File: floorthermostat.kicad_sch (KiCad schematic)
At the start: 26 parts, among them J1 Conn_01x03_Socket, J2 spi7segdisp, J3 ProgLoad, Q1 BC549, SW1 SW_Push, SW2 SW_Push, U1 ESP32-WROOM-32, U2 S202S02, U3 BD33FC0FP, U4 DS18B20

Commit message: Added labels for esp, about the spi display.
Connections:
- net CLK: now also U1.30 (IO18)
- net DIN: now also U1.31 (IO19)
- net LOAD: now also U1.29 (IO5)
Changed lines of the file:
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@@
+	(wire
+		(pts
+			(xy 128.27 80.01) (xy 135.89 80.01)
+		)
+		(stroke
+			(width 0)
+			(type default)
+		)
+	)
 	(wire
 		(pts
@@
 	(wire
 		(pts
+			(xy 128.27 82.55) (xy 135.89 82.55)
+		)
+		(stroke
+			(width 0)
+			(type default)
+		)
+	)
+	(wire
+		(pts
 			(xy 175.26 72.39) (xy 175.26 76.2)
 		)
@@
 		(pts
 			(xy 200.66 36.83) (xy 213.36 36.83)
+		)
+		(stroke
+			(width 0)
+			(type default)
+		)
+	)
+	(wire
+		(pts
+			(xy 128.27 62.23) (xy 135.89 62.23)
 		)
 		(stroke
@@
 		)
 	)
+	(label "LOAD"
+		(at 135.89 62.23 180)
+		(fields_autoplaced yes)
+		(effects
+			(font
+				(size 1.27 1.27)
+			)
+			(justify right bottom)
+		)
+	)
 	(label "SETUP"
 		(at 135.89 67.31 180)
@@
 		)
 	)
+	(label "CLK"
+		(at 135.89 80.01 180)
+		(fields_autoplaced yes)
+		(effects
+			(font
+				(size 1.27 1.27)
+			)
+			(justify right bottom)
+		)
+	)
 	(label "TXD0/IO1"
 		(at 213.36 36.83 180)
@@
 		(fields_autoplaced yes)
 		(effects
+			(font
+				(size 1.27 1.27)
+			)
+			(justify right bottom)
+		)
+	)
+	(label "DIN"
+		(at 135.89 82.55 180)
+		(fields_autoplaced yes)
+		(effects

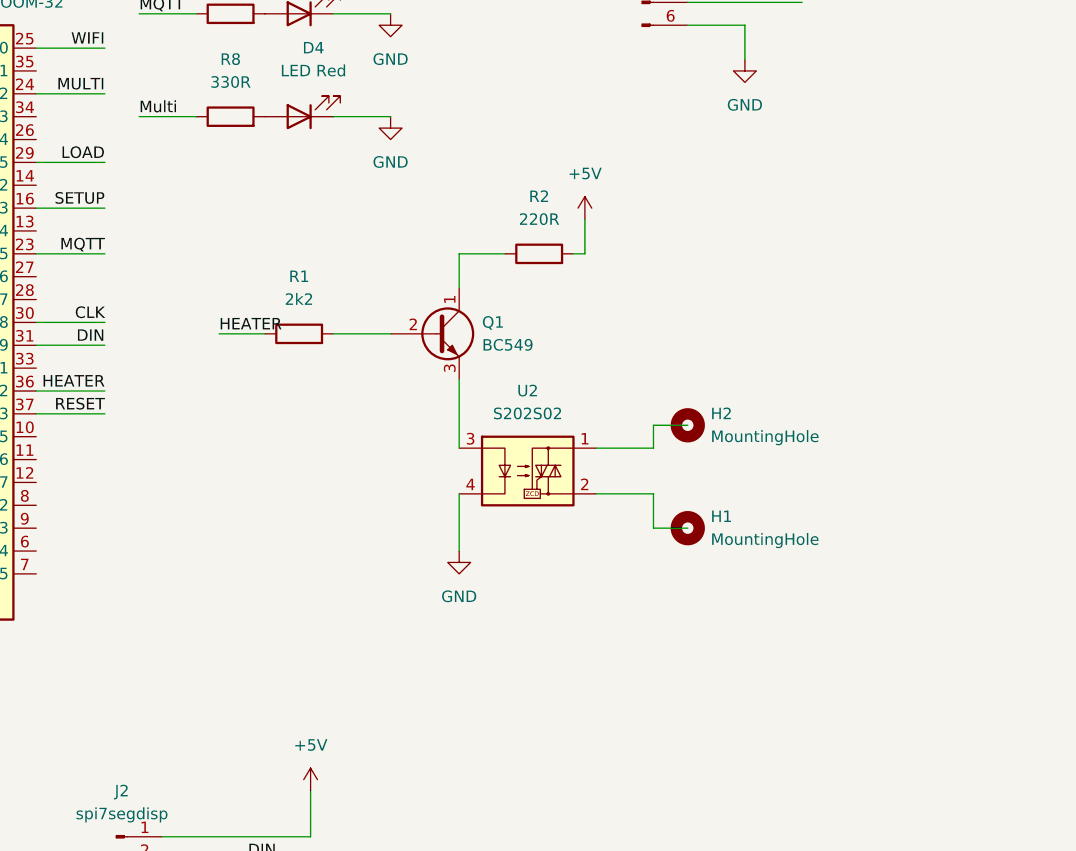
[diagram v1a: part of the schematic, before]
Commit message: Added ldr for display brightness control.
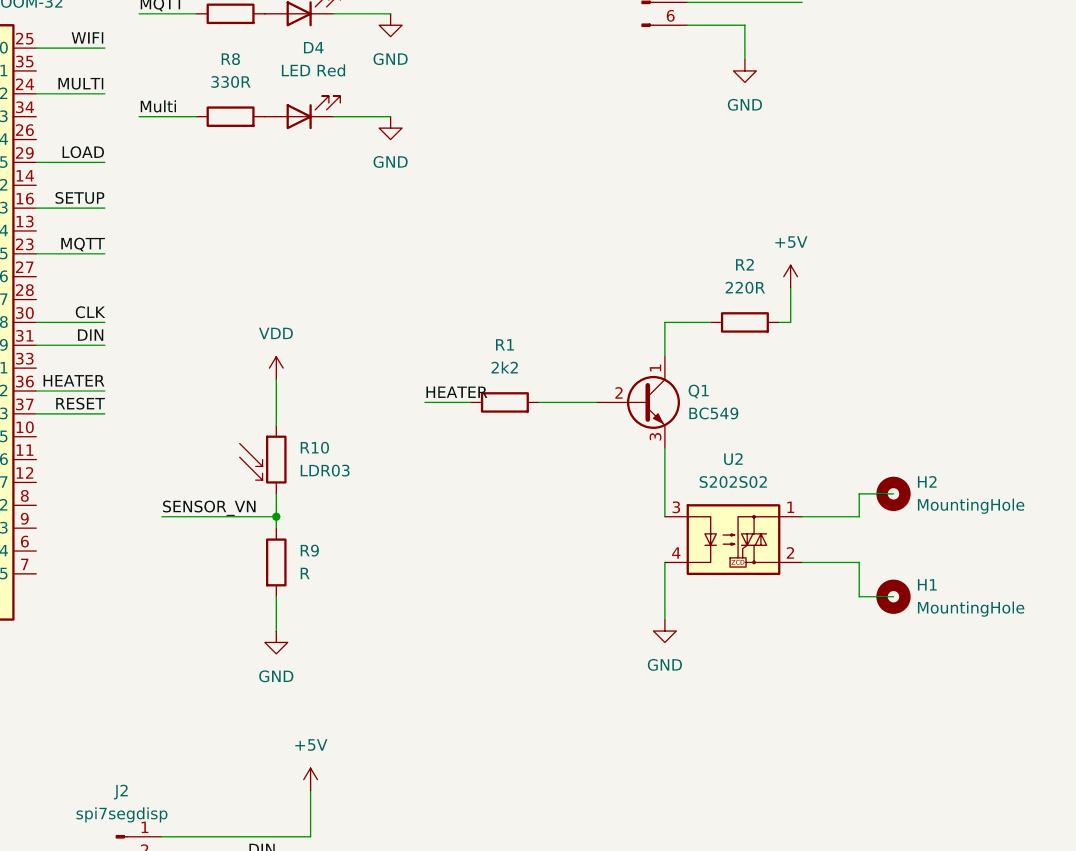
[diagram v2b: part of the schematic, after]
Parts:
- added R10: LDR03, OptoDevice:R_LDR_10x8.5mm_P7.6mm_Vertical, symbol Sensor_Optical:LDR03
- added R9: R, symbol Device:R
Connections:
- net GND: now also R9.2
- net VDD: now also R10.1
- new net SENSOR_VN: R10.2, R9.1
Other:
- moved on the sheet: H1, H2, Q1, R1, R2, U2

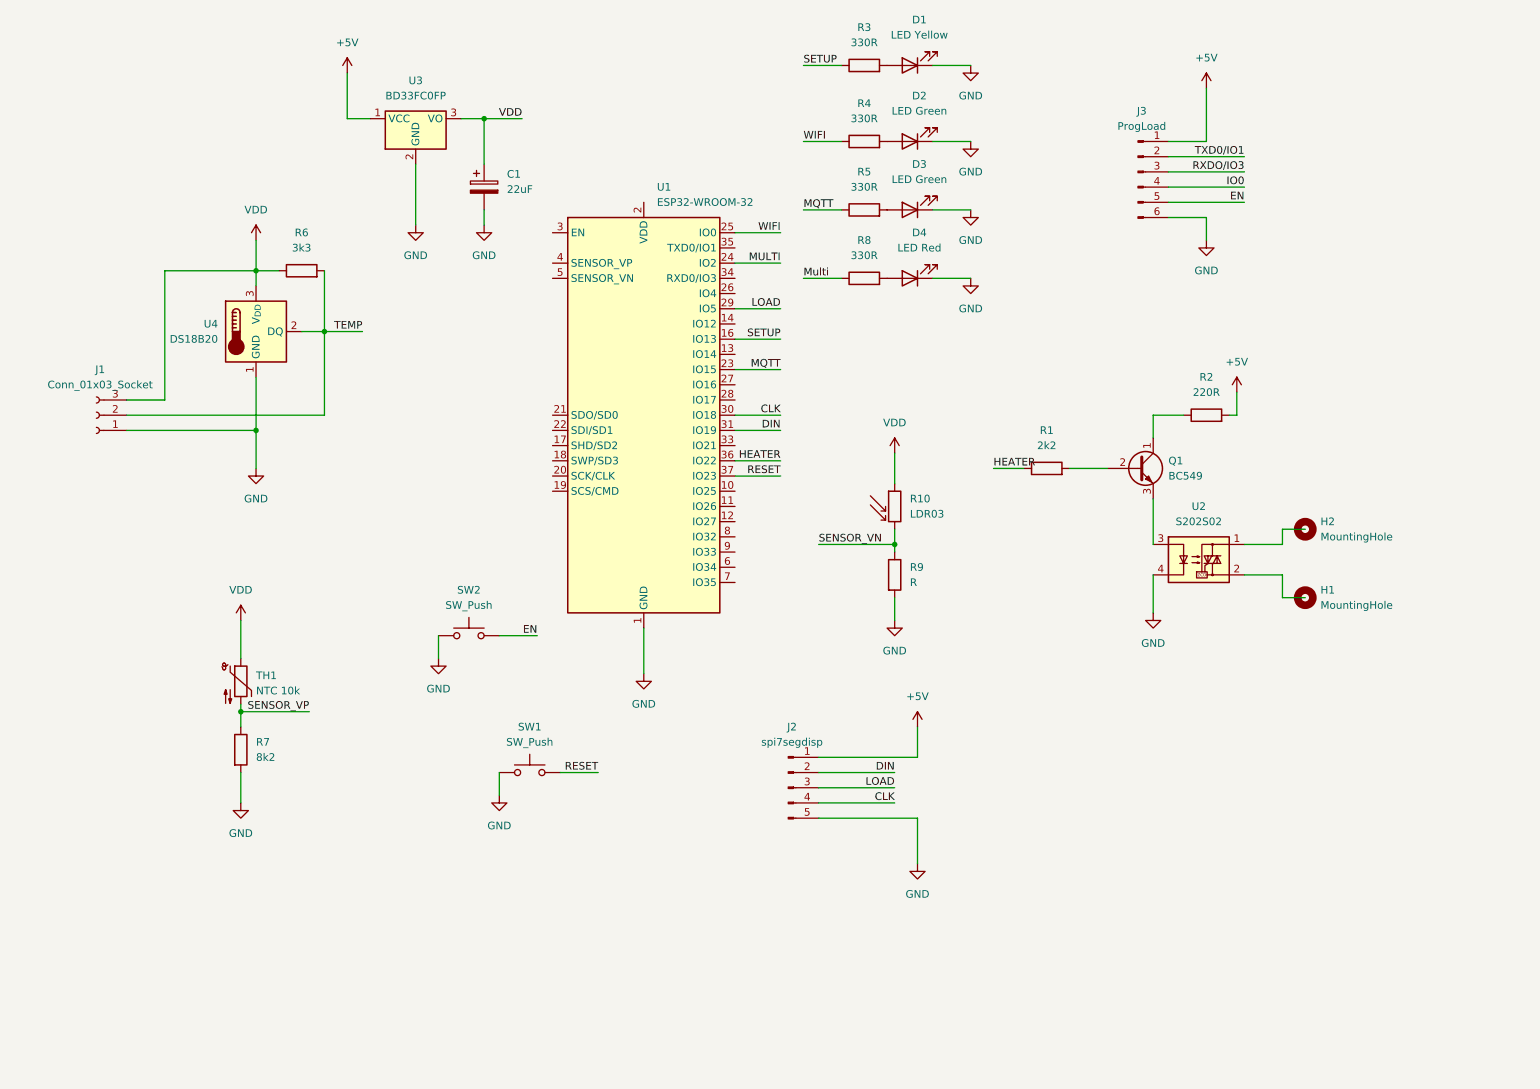
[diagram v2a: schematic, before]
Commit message: fixed ssr control bug. Added 2 filtering capasitors. Defined some component footprints.
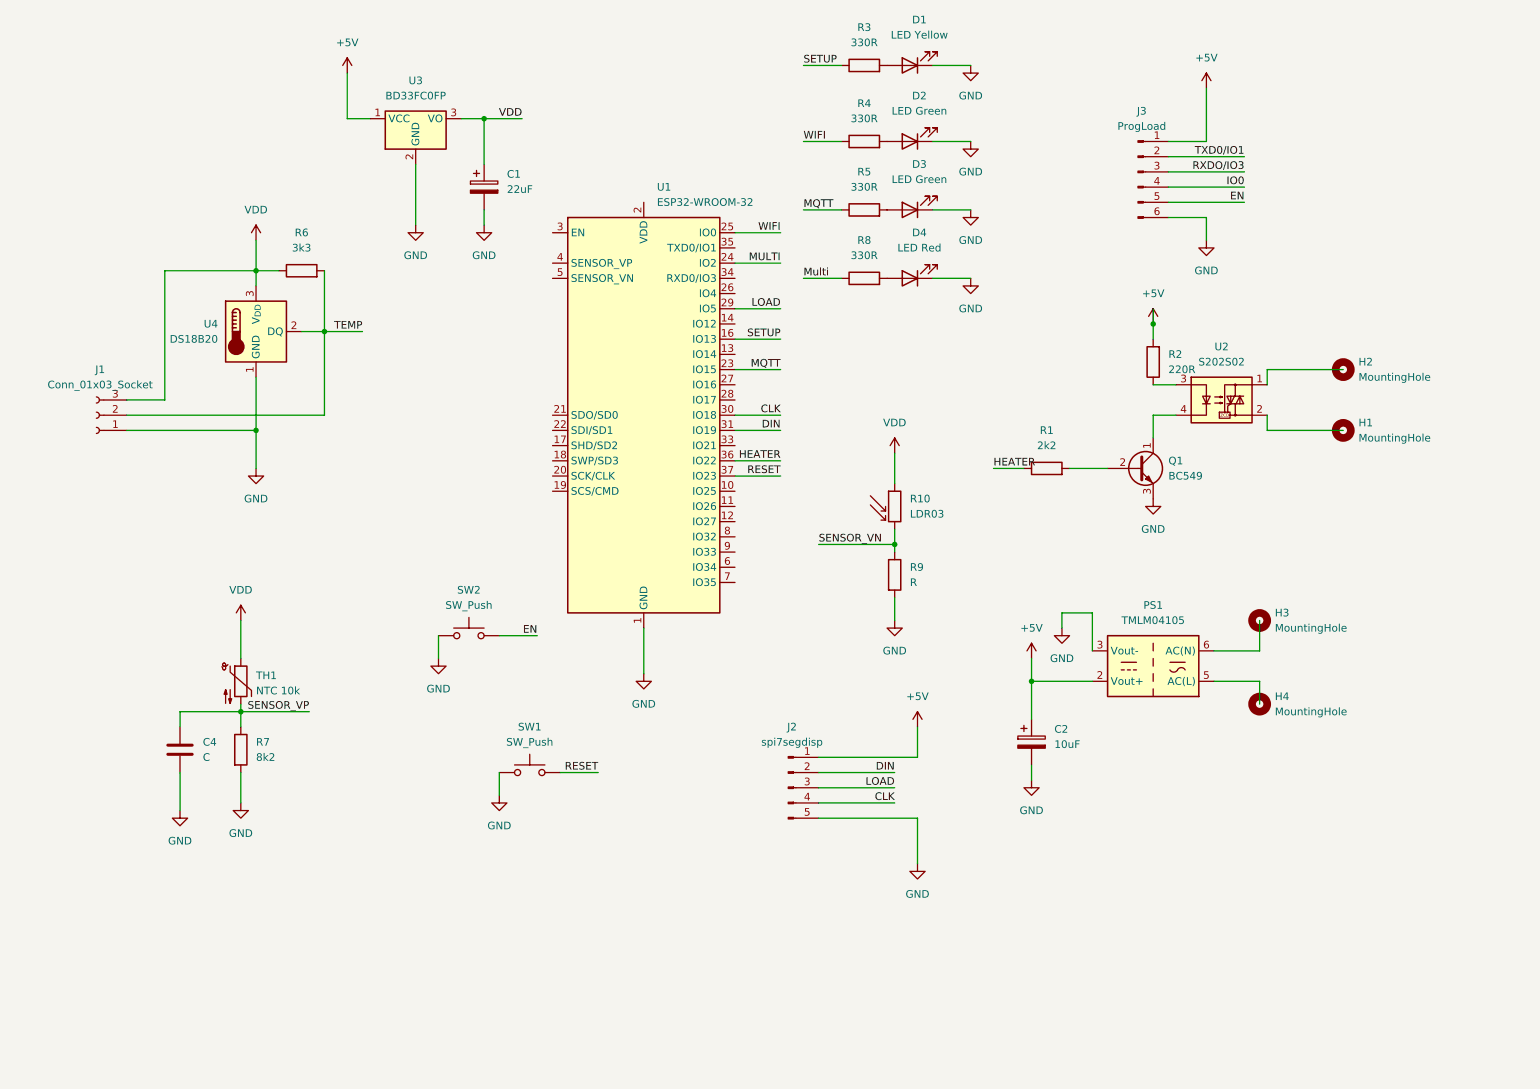
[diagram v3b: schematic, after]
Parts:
- added C2: 10uF, Capacitor_THT:CP_Axial_L10.0mm_D4.5mm_P15.00mm_Horizontal, symbol Device:C_Polarized
- added C4: C, Capacitor_THT:CP_Axial_L10.0mm_D6.0mm_P15.00mm_Horizontal, symbol Device:C
- added H3, H4: MountingHole, symbol Mechanical:MountingHole
- added PS1: TMLM04105, Converter_ACDC:Converter_ACDC_TRACO_TMLM-04_THT, symbol Converter_ACDC:TMLM04105
- C1: footprint (none) -> Capacitor_THT:CP_Axial_L10.0mm_D4.5mm_P15.00mm_Horizontal
- D1, D2, D3, D4: footprint (none) -> LED_THT:LED_D5.0mm
- R1: footprint (none) -> Resistor_THT:R_Axial_DIN0207_L6.3mm_D2.5mm_P15.24mm_Horizontal
- R2, R3, R4, R5, R6, R7, R8, R9: footprint (none) -> Resistor_THT:R_Axial_DIN0207_L6.3mm_D2.5mm_P2.54mm_Vertical
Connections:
- net +5V: now also C2.1, PS1.2 (Vout+)
- net GND: now also Q1.3 (E), C2.2, C4.2, PS1.3 (Vout-); no longer U2.4
- net SENSOR_VP: now also C4.1
- net at R2.1: now also U2.3; no longer Q1.1 (C)
- new net: Q1.1 (C), U2.4
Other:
- moved on the sheet: H1, H2, R2, U2

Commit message: Added many footprints.
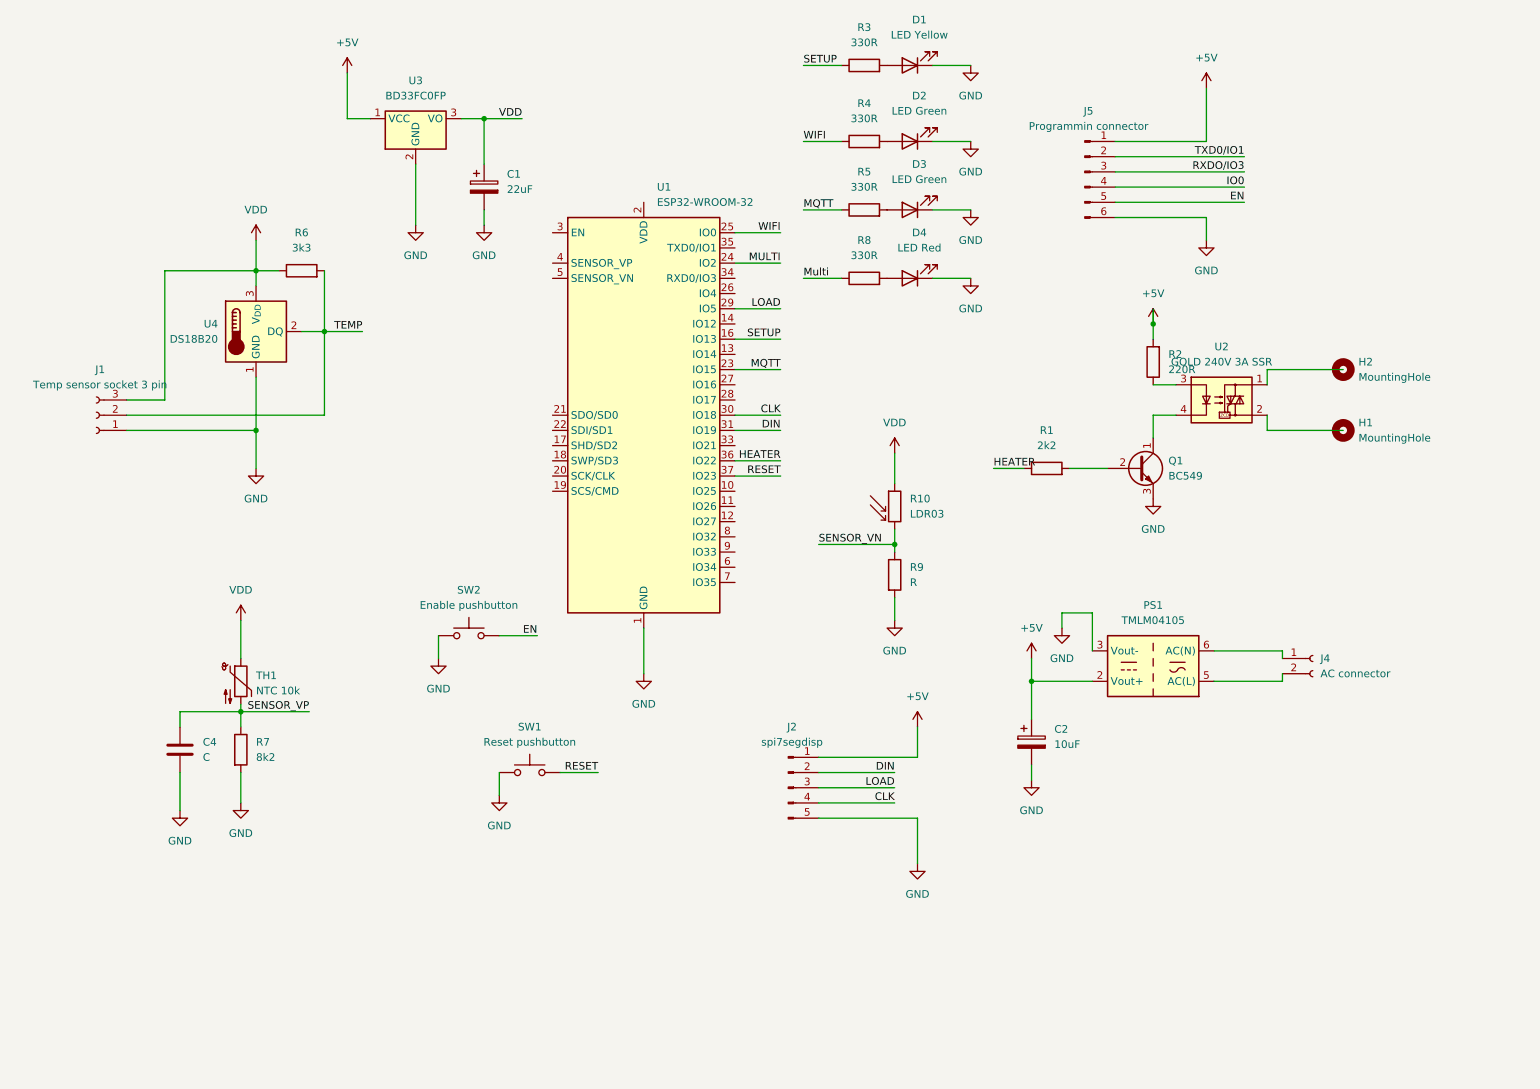
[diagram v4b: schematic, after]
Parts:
- removed H3, H4: MountingHole, symbol Mechanical:MountingHole
- removed J3: ProgLoad, symbol Connector:Conn_01x06_Pin
- added J4: AC connector, symbol Connector:Conn_01x02_Socket
- added J5: Programmin connector, Connector_PinHeader_2.54mm:PinHeader_1x06_P2.54mm_Vertical, symbol Connector:Conn_01x06_Pin
- H1: footprint (none) -> customparts:china_5v_acdc
- H2: footprint (none) -> Relay_THT:Relay_NCR_HHG1D-1
- J1: value Conn_01x03_Socket -> Temp sensor socket 3 pin; footprint (none) -> Connector_PinSocket_2.54mm:PinSocket_1x03_P2.54mm_Horizontal
- J2: footprint (none) -> Connector_PinHeader_2.54mm:PinHeader_1x05_P2.54mm_Vertical
- PS1: footprint Converter_ACDC:Converter_ACDC_TRACO_TMLM-04_THT -> customparts:china_5v_acdc
- SW1: value SW_Push -> Reset pushbutton; footprint (none) -> Button_Switch_THT:SW_PUSH_6mm_H5mm
- SW2: value SW_Push -> Enable pushbutton; footprint (none) -> Button_Switch_THT:SW_PUSH_6mm_H5mm
- U2: value S202S02 -> GOLD 240V 3A SSR; footprint Package_SIP:SIP4_Sharp-SSR_P7.62mm_Straight -> Relay_THT:Relay_NCR_HHG1D-1
- U3: footprint Package_TO_SOT_SMD:TO-252-2 -> Package_TO_SOT_THT:TO-262-3_Vertical
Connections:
- net +5V: now also J5.1 (Pin_1)
- net EN: now also J5.5 (Pin_5)
- net GND: now also J5.6 (Pin_6)
- net IO0: now also J5.4 (Pin_4)
- net RXDO/IO3: now also J5.3 (Pin_3)
- net TXD0/IO1: now also J5.2 (Pin_2)
- net at PS1.5 (AC(L)): now also J4.2 (Pin_2)
- net at PS1.6 (AC(N)): now also J4.1 (Pin_1)

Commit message: Created footprint for GOLD_SSR_3A relay. Added 6 pin screw header for ac, heater and ntc.
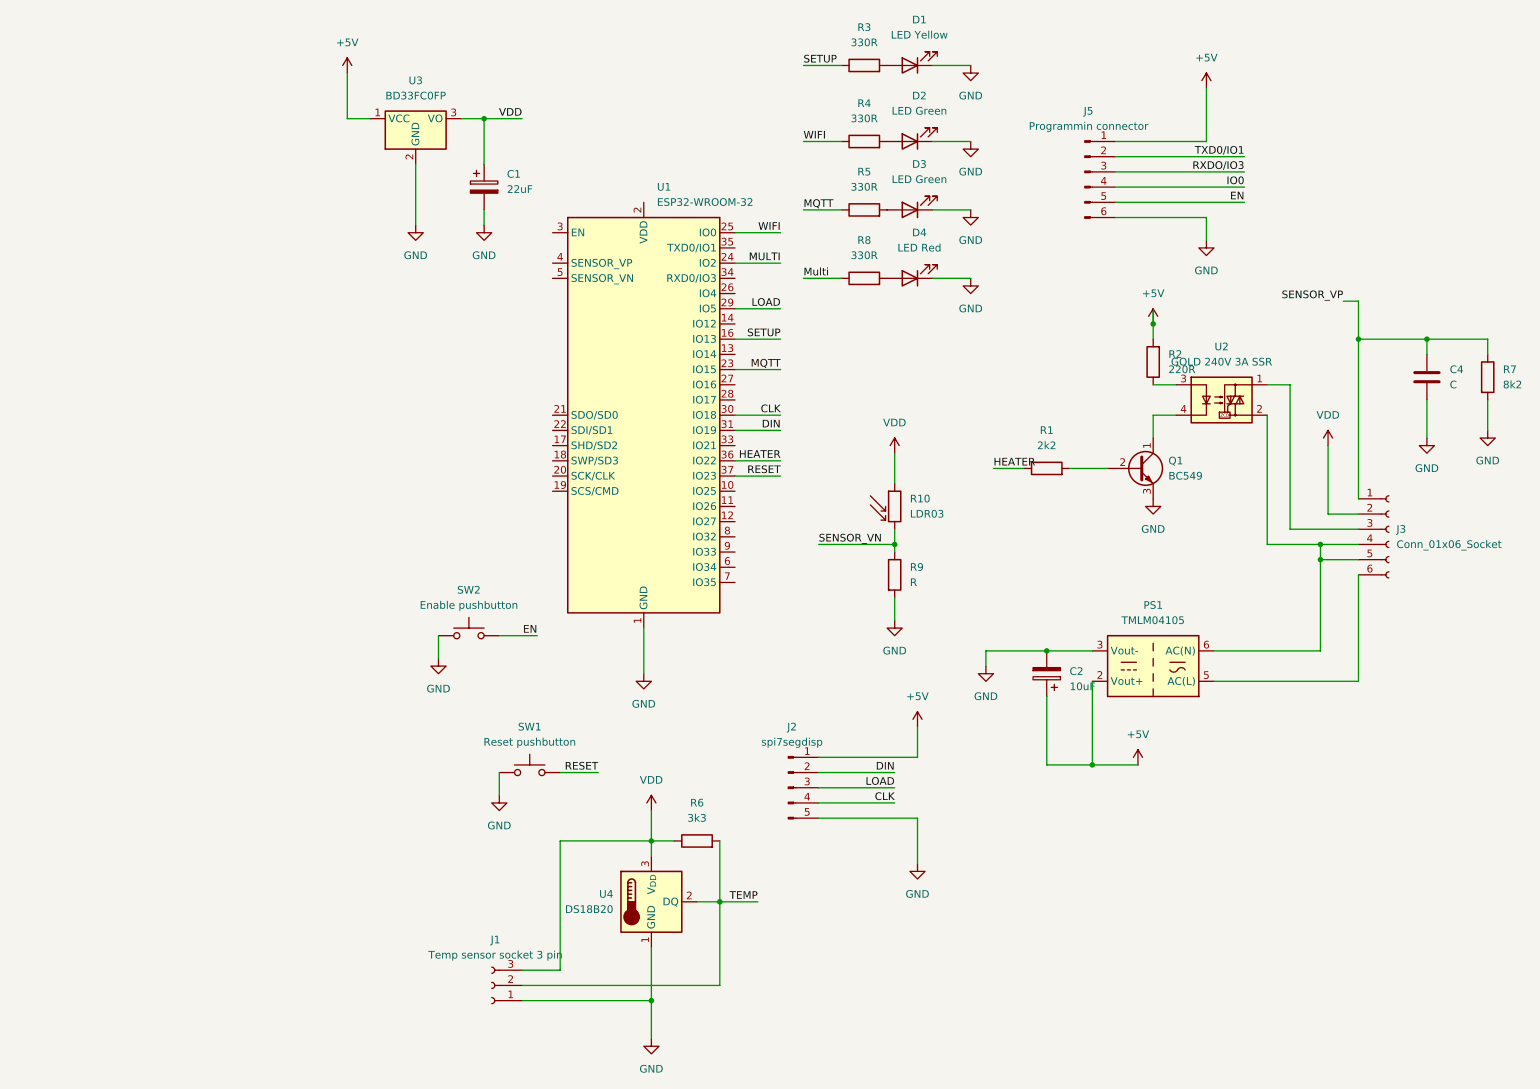
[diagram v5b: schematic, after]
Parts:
- removed H1: MountingHole, customparts:china_5v_acdc, symbol Mechanical:MountingHole
- removed H2: MountingHole, Relay_THT:Relay_NCR_HHG1D-1, symbol Mechanical:MountingHole
- removed J4: AC connector, symbol Connector:Conn_01x02_Socket
- removed TH1: NTC 10k, symbol Device:Thermistor_NTC
- added J3: Conn_01x06_Socket, TerminalBlock_Phoenix:TerminalBlock_Phoenix_MKDS-1,5-6-5.08_1x06_P5.08mm_Horizontal, symbol Connector:Conn_01x06_Socket
- U2: footprint Relay_THT:Relay_NCR_HHG1D-1 -> customparts:Relay_GOLD_3A
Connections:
- net SENSOR_VP: now also J3.1 (Pin_1)
- net VDD: now also J3.2 (Pin_2)
- net at PS1.6 (AC(N)): now also U2.2, J3.4 (Pin_4), J3.5 (Pin_5)
- net at PS1.5 (AC(L)): now also J3.6 (Pin_6)
- net at U2.1: now also J3.3 (Pin_3)
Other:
- moved on the sheet: C2, C4, J1, R6, R7, U4
